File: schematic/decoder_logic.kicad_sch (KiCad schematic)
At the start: 2 parts, among them U5 74LS138, U6 74LS138

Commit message: cleanup, and started associating components
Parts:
- U5, U6: footprint (none) -> Package_DIP:DIP-16_W7.62mm_LongPads
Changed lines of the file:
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@@
   (symbol (lib_id "power:GNDD") (at 144.78 85.09 0) (unit 1)
     (in_bom yes) (on_board yes) (fields_autoplaced)
-    (property "Reference" "#PWR?" (id 0) (at 144.78 91.44 0)
+    (property "Reference" "#PWR0230" (id 0) (at 144.78 91.44 0)
       (effects (font (size 1.27 1.27)) hide)
     )
@@
   (symbol (lib_id "power:+5V") (at 144.78 98.425 0) (unit 1)
     (in_bom yes) (on_board yes) (fields_autoplaced)
-    (property "Reference" "#PWR?" (id 0) (at 144.78 102.235 0)
+    (property "Reference" "#PWR0231" (id 0) (at 144.78 102.235 0)
       (effects (font (size 1.27 1.27)) hide)
     )
@@
       (effects (font (size 1.27 1.27)) (justify left))
     )
-    (property "Footprint" "" (id 2) (at 144.78 67.31 0)
+    (property "Footprint" "Package_DIP:DIP-16_W7.62mm_LongPads" (id 2) (at 144.78 67.31 0)
       (effects (font (size 1.27 1.27)) hide)
     )
@@
   (symbol (lib_id "power:GNDD") (at 144.78 131.445 0) (unit 1)
     (in_bom yes) (on_board yes) (fields_autoplaced)
-    (property "Reference" "#PWR?" (id 0) (at 144.78 137.795 0)
+    (property "Reference" "#PWR0232" (id 0) (at 144.78 137.795 0)
       (effects (font (size 1.27 1.27)) hide)
     )
@@
   (symbol (lib_id "power:+5V") (at 144.78 52.07 0) (unit 1)
     (in_bom yes) (on_board yes) (fields_autoplaced)
-    (property "Reference" "#PWR?" (id 0) (at 144.78 55.88 0)
+    (property "Reference" "#PWR0229" (id 0) (at 144.78 55.88 0)
       (effects (font (size 1.27 1.27)) hide)
     )
@@
       (effects (font (size 1.27 1.27)) (justify left))
     )
-    (property "Footprint" "" (id 2) (at 144.78 113.665 0)
+    (property "Footprint" "Package_DIP:DIP-16_W7.62mm_LongPads" (id 2) (at 144.78 113.665 0)
       (effects (font (size 1.27 1.27)) hide)
     )

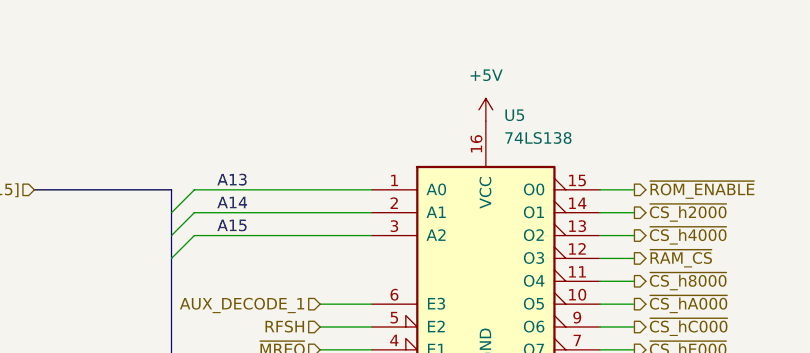
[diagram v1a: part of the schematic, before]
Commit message: first draft of board with components added, no traces
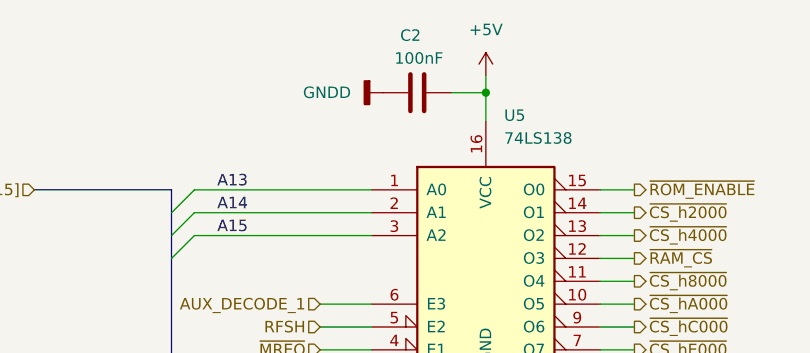
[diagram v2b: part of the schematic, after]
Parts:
- added C2: 100nF, Capacitor_THT:C_Disc_D7.0mm_W2.5mm_P5.00mm, symbol Device:C
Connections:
- net +5V: now also C2.1
- net GNDD: now also C2.2
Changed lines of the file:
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@@
     (comment 1 "Jay Convertino")
+  )
+  (junction (at 144.78 48.895) (diameter 0) (color 0 0 0 0)
   )
   (no_connect (at 157.48 118.745))
@@
     (stroke (width 0) (type default) (color 0 0 0 0))
   )
+  (wire (pts (xy 144.78 46.99) (xy 144.78 48.895))
+    (stroke (width 0) (type default) (color 0 0 0 0))
+  )
+  (wire (pts (xy 140.97 48.895) (xy 144.78 48.895))
+    (stroke (width 0) (type default) (color 0 0 0 0))
+  )
   (wire (pts (xy 157.48 62.23) (xy 161.29 62.23))
     (stroke (width 0) (type default) (color 0 0 0 0))
@@
   )
   (wire (pts (xy 127 123.825) (xy 132.08 123.825))
+    (stroke (width 0) (type default) (color 0 0 0 0))
+  )
+  (wire (pts (xy 144.78 48.895) (xy 144.78 52.07))
     (stroke (width 0) (type default) (color 0 0 0 0))
   )
@@
     (pin "1")
   )
-  (symbol (lib_id "power:+5V") (at 144.78 52.07 0) (unit 1)
-    (in_bom yes) (on_board yes) (fields_autoplaced)
-    (property "Reference" "#PWR0229" (id 0) (at 144.78 55.88 0)
-      (effects (font (size 1.27 1.27)) hide)
-    )
-    (property "Value" "+5V" (id 1) (at 144.78 46.99 0))
-    (property "Footprint" "" (id 2) (at 144.78 52.07 0)
-      (effects (font (size 1.27 1.27)) hide)
-    )
-    (property "Datasheet" "" (id 3) (at 144.78 52.07 0)
+  (symbol (lib_id "power:+5V") (at 144.78 46.99 0) (unit 1)
+    (in_bom yes) (on_board yes) (fields_autoplaced)
+    (property "Reference" "#PWR0229" (id 0) (at 144.78 50.8 0)
+      (effects (font (size 1.27 1.27)) hide)
+    )
+    (property "Value" "+5V" (id 1) (at 144.78 41.91 0))
+    (property "Footprint" "" (id 2) (at 144.78 46.99 0)
+      (effects (font (size 1.27 1.27)) hide)
+    )
+    (property "Datasheet" "" (id 3) (at 144.78 46.99 0)
+      (effects (font (size 1.27 1.27)) hide)
+    )
+    (pin "1")
+  )
+  (symbol (lib_id "power:GNDD") (at 133.35 48.895 270) (unit 1)
+    (in_bom yes) (on_board yes)
+    (property "Reference" "#PWR0263" (id 0) (at 127 48.895 0)
+      (effects (font (size 1.27 1.27)) hide)
+    )
+    (property "Value" "GNDD" (id 1) (at 124.46 48.895 90)
+      (effects (font (size 1.27 1.27)) (justify left))
+    )
+    (property "Footprint" "" (id 2) (at 133.35 48.895 0)
+      (effects (font (size 1.27 1.27)) hide)
+    )
+    (property "Datasheet" "" (id 3) (at 133.35 48.895 0)
       (effects (font (size 1.27 1.27)) hide)
     )
@@
     (pin "9")
   )
+  (symbol (lib_id "Device:C") (at 137.16 48.895 270) (unit 1)
+    (in_bom yes) (on_board yes)
+    (property "Reference" "C2" (id 0) (at 135.255 42.545 90)
+      (effects (font (size 1.27 1.27)) (justify left))
+    )
+    (property "Value" "100nF" (id 1) (at 134.62 45.085 90)
+      (effects (font (size 1.27 1.27)) (justify left))
+    )
+    (property "Footprint" "Capacitor_THT:C_Disc_D7.0mm_W2.5mm_P5.00mm" (id 2) (at 133.35 49.8602 0)
+      (effects (font (size 1.27 1.27)) hide)
+    )
+    (property "Datasheet" "~" (id 3) (at 137.16 48.895 0)
+      (effects (font (size 1.27 1.27)) hide)
+    )
+    (pin "1")
+    (pin "2")
+  )
 )

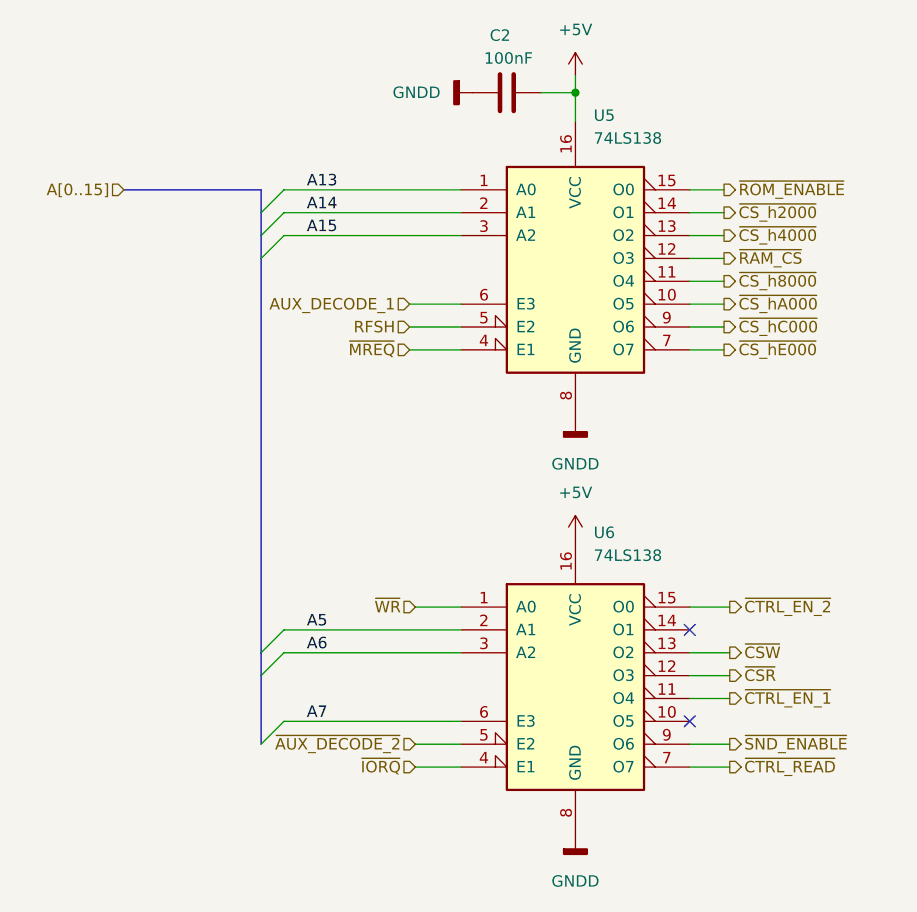
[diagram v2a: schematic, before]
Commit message: fixed a bug on the +5v line, added +5NF (no filter) net list names. Added traces to the ram, and inverter, and select ics.
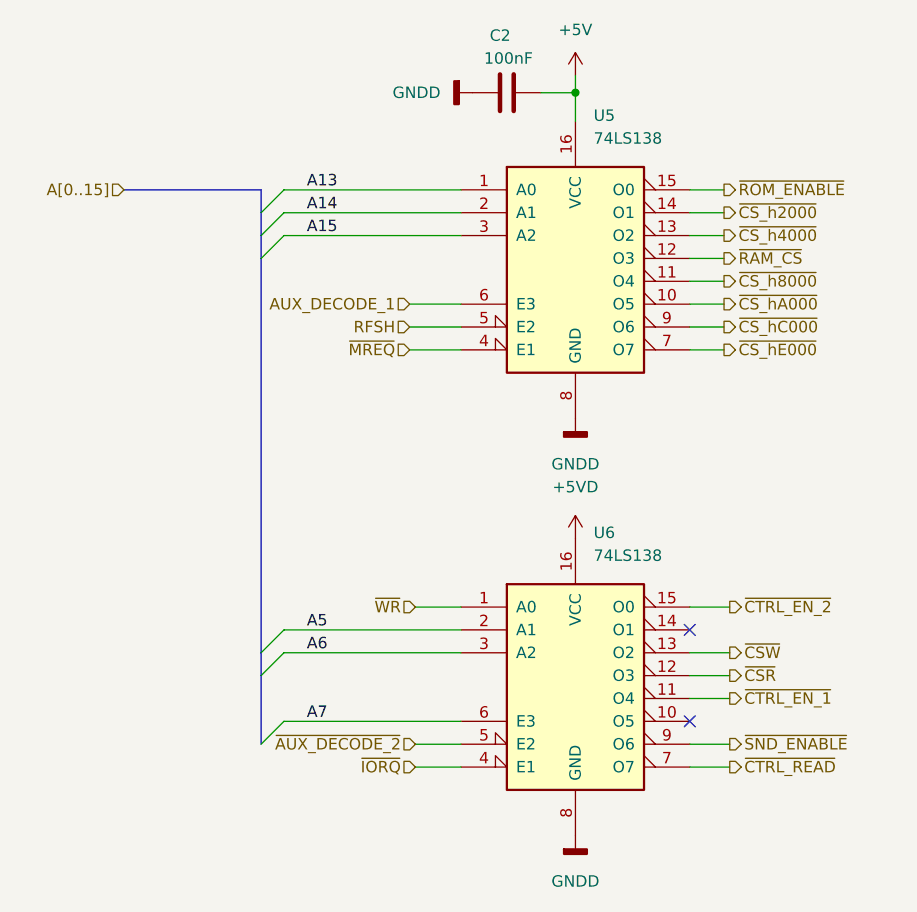
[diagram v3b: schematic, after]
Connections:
- net +5V: no longer U6.16 (VCC)
- new net +5VD: U6.16 (VCC)
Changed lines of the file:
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@@
     (pin "1")
   )
-  (symbol (lib_id "power:+5V") (at 144.78 98.425 0) (unit 1)
+  (symbol (lib_id "power:+5VD") (at 144.78 98.425 0) (unit 1)
     (in_bom yes) (on_board yes) (fields_autoplaced)
     (property "Reference" "#PWR0231" (id 0) (at 144.78 102.235 0)
       (effects (font (size 1.27 1.27)) hide)
     )
-    (property "Value" "+5V" (id 1) (at 144.78 93.345 0))
+    (property "Value" "+5VD" (id 1) (at 144.78 92.71 0))
     (property "Footprint" "" (id 2) (at 144.78 98.425 0)
       (effects (font (size 1.27 1.27)) hide)

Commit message: updated schematic with new layout
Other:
- company: (none) -> sparkletron
- title: Colecovision Schematic -> Reverse Engineer Colecovision
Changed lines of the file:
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@@
   (paper "USLetter")
   (title_block
-    (title "Colecovision Schematic")
-    (date "2023-01-09")
-    (rev "F.0")
+    (title "Reverse Engineer Colecovision")
+    (date "2023-03-14")
+    (rev "DEV")
+    (company "sparkletron")
     (comment 1 "Jay Convertino")
+    (comment 2 "MIT LICENSE")
   )
   (junction (at 144.78 48.895) (diameter 0) (color 0 0 0 0)
